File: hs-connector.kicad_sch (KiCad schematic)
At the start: 48 parts, among them J2001 Socket_Samtec_ERF8_2x25_ERF8-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, T2001 Choke_DLW21SN900HQ2L, T2002 Choke_DLW21SN900HQ2L, T2003 Choke_DLW21SN900HQ2L, U2001 SN65MLVD200A, U2002 74AVC4T245_UQFN

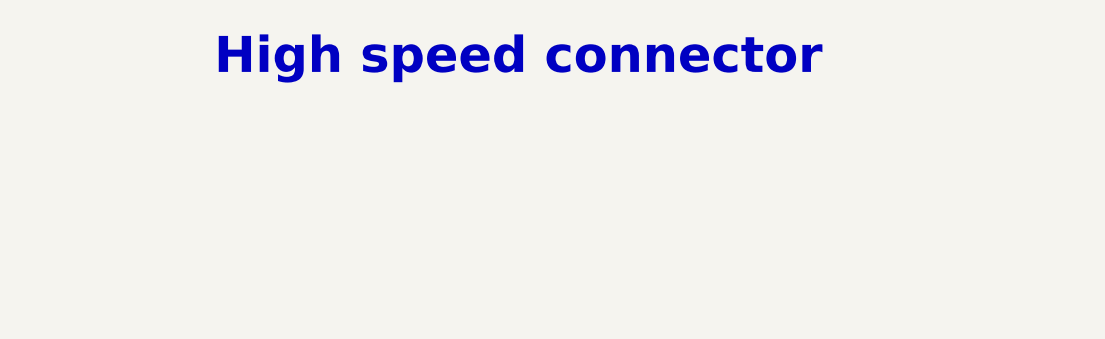
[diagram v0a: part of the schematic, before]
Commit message: [#100282] Add missing schematic sheet names and align them all
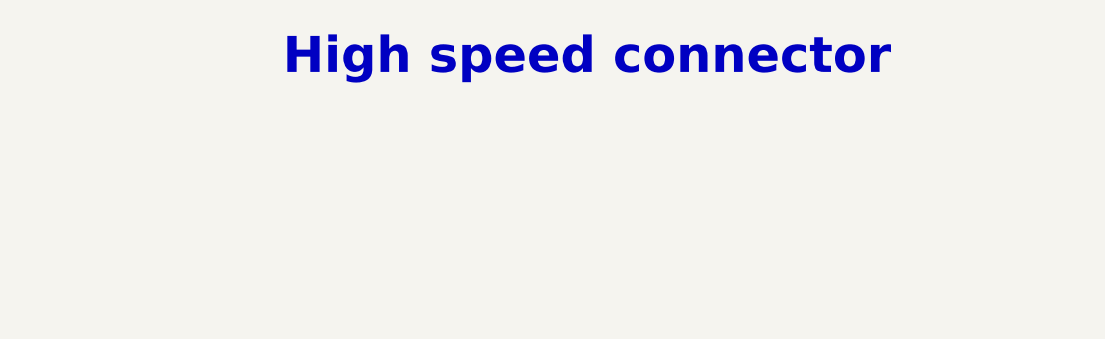
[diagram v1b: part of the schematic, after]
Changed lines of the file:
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@@
 	(text "High speed connector"
 		(exclude_from_sim no)
-		(at 203.2 38.1 0)
+		(at 210.82 38.1 0)
 		(effects
 			(font

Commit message: [#100501] Reannotate schematic
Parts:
- renumbered C2019 to C181, C2020 to C182, C2005 to C183, C2006 to C184, C2007 to C185, C2008 to C186, C2009 to C187, C2001 to C188, C2003 to C189, C2002 to C190, C2004 to C191, C2010 to C192, C2011 to C193, C2012 to C194, C2013 to C195, C2014 to C196, C2015 to C197, C2016 to C198, C2017 to C199, C2018 to C200, D2001 to D1, F2001 to F1, J2001 to J6, R2019 to R219, R2001 to R220, R2002 to R221, R2003 to R222, R2004 to R223, R2005 to R224, R2006 to R225, R2007 to R226, R2008 to R227, R2009 to R228, R2010 to R229, R2011 to R230, R2012 to R231, R2013 to R232, R2014 to R233, R2015 to R234, R2016 to R235, R2017 to R236, R2018 to R237, R2020 to R238, T2001 to T1, T2002 to T2, T2003 to T3, U2002 to U27, U2001 to U28

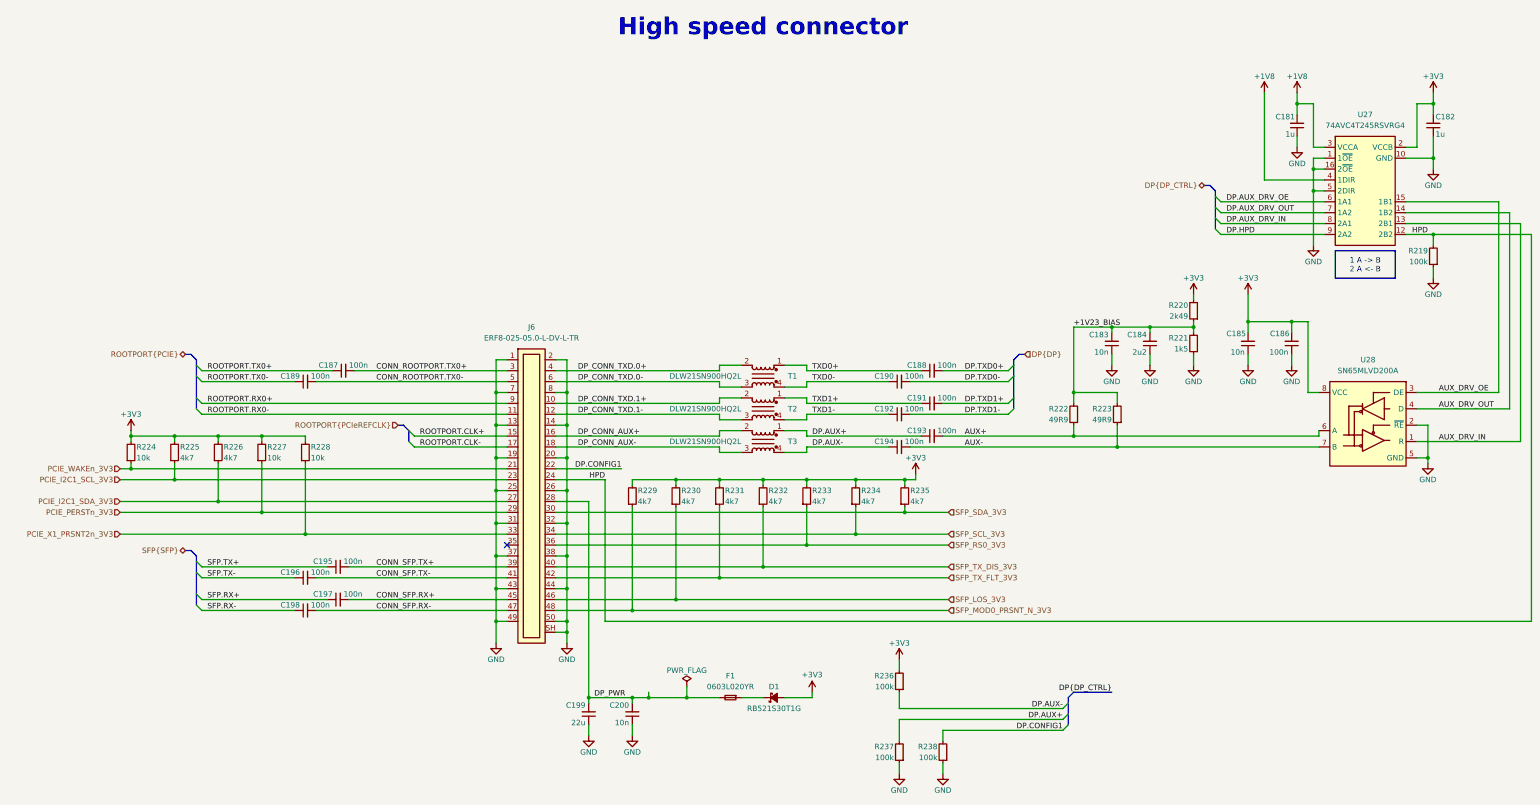
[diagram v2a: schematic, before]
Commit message: [#100595] Update connections according to client request
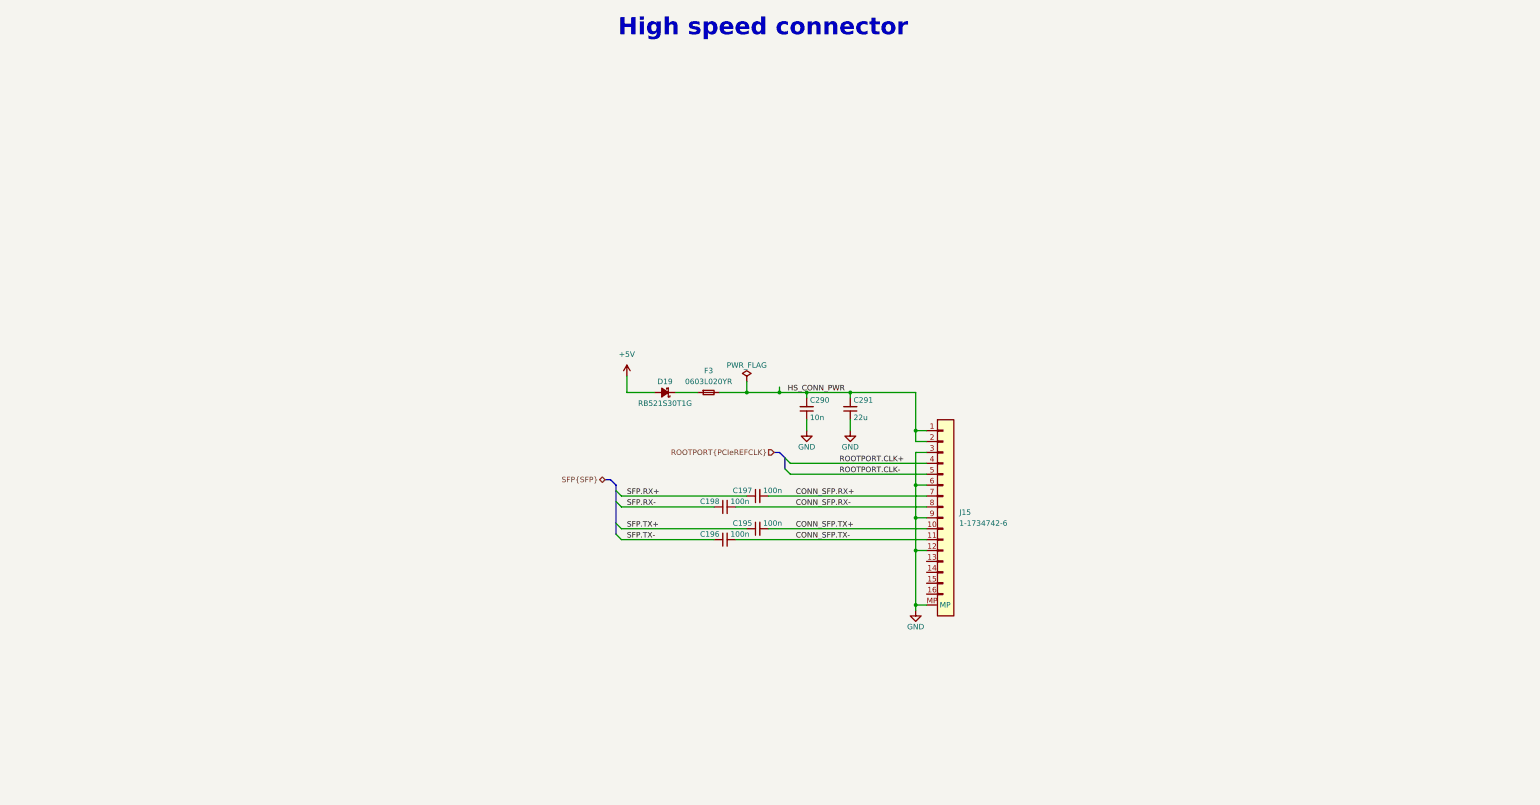
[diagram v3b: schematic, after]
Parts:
- removed C181, C182: C_1u_0402, antmicro-footprints:C_0402_1005Metric, symbol antmicroCapacitors0402:C_1u_0402
- removed C183, C185, C200: C_10n_0402, antmicro-footprints:C_0402_1005Metric, symbol antmicroCapacitors0402:C_10n_0402
- removed C184: C_2u2_0402, antmicro-footprints:C_0402_1005Metric, symbol antmicroCapacitors0402:C_2u2_0402
- removed C186, C187, C188, C189, C190, C191, C192, C193, C194: C_100n_0402, antmicro-footprints:C_0402_1005Metric, symbol antmicroCapacitors0402:C_100n_0402
- removed C199: C_22u_16V_0603, antmicro-footprints:C_0603_1608Metric_EIA, symbol antmicroCapacitors0603:C_22u_16V_0603
- removed D1: RB521S30T1G, antmicro-footprints:SOD-523, symbol antmicroDiodesRectifiersSingle:RB521S30T1G
- removed F1: PTC_500mA_0603, antmicro-footprints:F_0603_1608Metric, symbol antmicroFuses:PTC_500mA_0603
- removed J6: Socket_Samtec_ERF8_2x25_ERF8-025-05.0-L-DV-L-TR, antmicro-footprints:Conn_Socket_Samtec_ERF8_2x25_ERF8-025-05.0-L-DV-L-TR, symbol antmicroB2BConnectors:Socket_Samtec_ERF8_2x25_ERF8-025-05.0-L-DV-L-TR
- removed R219, R236, R237, R238: R_100k_0402, antmicro-footprints:R_0402_1005Metric, symbol antmicroResistors0402:R_100k_0402
- removed R220: R_2k49_0402, antmicro-footprints:R_0402_1005Metric, symbol antmicroResistors0402:R_2k49_0402
- removed R221: R_1k5_0402, antmicro-footprints:R_0402_1005Metric, symbol antmicroResistors0402:R_1k5_0402
- removed R222, R223: R_49R9_0402, antmicro-footprints:R_0402_1005Metric, symbol antmicroResistors0402:R_49R9_0402
- removed R224, R227, R228: R_10k_0402, antmicro-footprints:R_0402_1005Metric, symbol antmicroResistors0402:R_10k_0402
- removed R225, R226, R229, R230, R231, R232, R233, R234, R235: R_4k7_0402, antmicro-footprints:R_0402_1005Metric, symbol antmicroResistors0402:R_4k7_0402
- removed T1, T2, T3: Choke_DLW21SN900HQ2L, antmicro-footprints:Choke_Murata-DLW21, symbol antmicroCommonModeChokes:Choke_DLW21SN900HQ2L
- removed U27: 74AVC4T245_UQFN, antmicro-footprints:UQFN-16-1.8x2.6mm_P0.4mm_Texas_RSV0016A, symbol antmicroLogicTranslatorsLevelShifters:74AVC4T245_UQFN
- removed U28: SN65MLVD200A, antmicro-footprints:SOIC-8_3.9x4.9x1.75mm_P1.27mm, symbol antmicroInterfaceDriversReceiversTransceivers:SN65MLVD200A
- added C290: C_10n_0402, antmicro-footprints:C_0402_1005Metric, symbol antmicroCapacitors0402:C_10n_0402
- added C291: C_22u_16V_0603, antmicro-footprints:C_0603_1608Metric_EIA, symbol antmicroCapacitors0603:C_22u_16V_0603
- added D19: RB521S30T1G, antmicro-footprints:SOD-523, symbol antmicroDiodesRectifiersSingle:RB521S30T1G
- added F3: PTC_500mA_0603, antmicro-footprints:F_0603_1608Metric, symbol antmicroFuses:PTC_500mA_0603
- added J15: FFC_TE_1-1734742-6, antmicro-footprints:Conn_FFC_TE_1-1734742-6, symbol antmicroFCCConnectors:FFC_TE_1-1734742-6
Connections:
- net CONN_SFP.RX+: now also J15.7
- net CONN_SFP.RX-: now also J15.8
- net CONN_SFP.TX+: now also J15.10
- net CONN_SFP.TX-: now also J15.11
- net GND: now also C290.1, C291.1, J15.12, J15.3, J15.6, J15.9, J15.MP
- net ROOTPORT.CLK+: now also J15.4
- net ROOTPORT.CLK-: now also J15.5
- new net: D19.1 (C), F3.1
- new net +5V: D19.2 (A)
- new net HS_CONN_PWR: C290.2, C291.2, F3.2, J15.1, J15.2
- no-connect marks 1 -> 0

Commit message: [#100595] Update HS connections
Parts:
- removed D19: RB521S30T1G, antmicro-footprints:SOD-523, symbol antmicroDiodesRectifiersSingle:RB521S30T1G
- added D23: RB521S30T1G, antmicro-footprints:SOD-523, symbol antmicroDiodesRectifiersSingle:RB521S30T1G
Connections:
- net +5V: now also D23.2 (A)
- net at F3.1: now also D23.1 (C)
- net PCIE_PWR_EN: now reaches J15.13
- net PCIE_DET_WAKE: now reaches J15.14
- net PCIE_CLKREQ_N: now reaches J15.15
- net PCIE_RST_B: now reaches J15.16
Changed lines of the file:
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@@
+	(wire
+		(pts
+			(xy 242.57 165.1) (xy 248.92 165.1)
+		)
+		(stroke
+			(width 0)
+			(type default)
+		)
+	)
 	(wire
 		(pts
@@
 	(wire
 		(pts
+			(xy 242.57 162.56) (xy 248.92 162.56)
+		)
+		(stroke
+			(width 0)
+			(type default)
+		)
+	)
+	(wire
+		(pts
 			(xy 212.09 147.32) (xy 248.92 147.32)
 		)
@@
 	(wire
 		(pts
+			(xy 242.57 167.64) (xy 248.92 167.64)
+		)
+		(stroke
+			(width 0)
+			(type default)
+		)
+	)
+	(wire
+		(pts
 			(xy 248.92 137.16) (xy 246.38 137.16)
 		)
@@
 		(pts
 			(xy 246.38 172.72) (xy 248.92 172.72)
+		)
+		(stroke
+			(width 0)
+			(type default)
+		)
+	)
+	(wire
+		(pts
+			(xy 242.57 170.18) (xy 248.92 170.18)
 		)
 		(stroke
@@
 		(shape bidirectional)
 		(at 173.99 143.51 180)
+		(effects
+			(font
+				(size 1.27 1.27)
+			)
+			(justify right)
+		)
+	)
+	(hierarchical_label "PCIE_PWR_EN"
+		(shape input)
+		(at 242.57 162.56 180)
+		(effects
+			(font
+				(size 1.27 1.27)
+			)
+			(justify right)
+		)
+	)
+	(hierarchical_label "PCIE_CLKREQ_N"
+		(shape input)
+		(at 242.57 167.64 180)
+		(effects
+			(font
+				(size 1.27 1.27)
+			)
+			(justify right)
+		)
+	)
+	(hierarchical_label "PCIE_DET_WAKE"
+		(shape input)
+		(at 242.57 165.1 180)
+		(effects
+			(font
+				(size 1.27 1.27)
+			)
+			(justify right)
+		)
+	)
+	(hierarchical_label "PCIE_RST_B"
+		(shape input)
+		(at 242.57 170.18 180)
 		(effects
 			(font
@@
 	)
 	(symbol
+		(lib_id "antmicroDiodesRectifiersSingle:RB521S30T1G")
+		(at 190.5 123.19 180)
+		(unit 1)
+		(body_style 1)
+		(exclude_from_sim no)
+		(in_bom yes)
+		(on_board yes)
+		(in_pos_files yes)
+		(dnp no)
+		(property "Reference" "D23"
+			(at 187.96 120.65 0)
+			(show_name no)
+			(do_not_autoplace no)
+			(effects
+				(font
+					(size 1.27 1.27)
+					(thickness 0.15)
+				)
+			)
+		)
+		(property "Value" "RB521S30T1G"
+			(at 167.64 107.95 0)
+			(hide yes)
+			(show_name no)
+			(do_not_autoplace no)
+			(effects
+				(font
+					(size 1.27 1.27)
+					(thickness 0.15)
+				)
+				(justify left bottom)
+			)
+		)
+		(property "Footprint" "antmicro-footprints:SOD-523"
+			(at 167.64 113.03 0)
+			(hide yes)
+			(show_name no)
+			(do_not_autoplace no)
+			(effects
+				(font
+					(size 1.27 1.27)
+					(thickness 0.15)
+				)
+				(justify left bottom)
+			)
+		)
+		(property "Datasheet" "https://www.onsemi.com/pdf/datasheet/rb521s30t1-d.pdf"
+			(at 167.64 110.49 0)
+			(hide yes)
+			(show_name no)
+			(do_not_autoplace no)
+			(effects
+				(font
+					(size 1.27 1.27)
+					(thickness 0.15)
+				)
+				(justify left bottom)
+			)
+		)
+		(property "Description" "Small Signal Schottky Diode, Single, 30 V, 200 mA, 500 mV, 1 A, 125 °C"
+			(at 190.5 123.19 0)
+			(hide yes)
+			(show_name no)
+			(do_not_autoplace no)
+			(effects
+				(font
+					(size 1.27 1.27)
+				)
+			)
+		)
+		(property "MPN" "RB521S30T1G"
+			(at 187.96 125.73 0)
+			(show_name no)
+			(do_not_autoplace no)
+			(effects
+				(font
+					(size 1.27 1.27)
+					(thickness 0.15)
+				)
+			)
+		)
+		(property "Manufacturer" "ON Semiconductor"
+			(at 167.64 105.41 0)
+			(hide yes)
+			(show_name no)
+			(do_not_autoplace no)
+			(effects
+				(font
+					(size 1.27 1.27)
+					(thickness 0.15)
+				)
+				(justify left bottom)
+			)
+		)
+		(property "Author" "Antmicro"
+			(at 167.64 102.87 0)
+			(hide yes)
+			(show_name no)
+			(do_not_autoplace no)
+			(effects
+				(font
+					(size 1.27 1.27)
+					(thickness 0.15)
+				)
+				(justify left bottom)
+			)
+		)
+		(property "License" "Apache-2.0"
+			(at 167.64 100.33 0)
+			(hide yes)
+			(show_name no)
+			(do_not_autoplace no)
+			(effects
+				(font
+					(size 1.27 1.27)
+					(thickness 0.15)
+				)
+				(justify left bottom)
+			)
+		)
+		(pin "1"
+		)
+		(pin "2"
+		)
+		(instances
+			(project "altera-modular-agilex-5-dc-scm"
+				(path "/6bb9d978-a328-4b30-874b-55170a976185/24358ccd-38f4-4473-b406-ebc28282868f"
+					(reference "D23")
+					(unit 1)
+				)
+			)
+		)
+	)
+	(symbol
 		(lib_id "antmicropower:GND")
 		(at 220.98 132.08 0)
@@
 					(unit 1)
 				)
-			)
-		)
-	)
-	(symbol
-		(lib_id "antmicroDiodesRectifiersSingle:RB521S30T1G")
-		(at 190.5 123.19 180)
-		(unit 1)
-		(body_style 1)
-		(exclude_from_sim no)
-		(in_bom yes)
-		(on_board yes)
-		(in_pos_files yes)
-		(dnp no)
-		(property "Reference" "D19"
-			(at 187.96 120.65 0)
-			(show_name no)
-			(do_not_autoplace no)
-			(effects
-				(font
-					(size 1.27 1.27)
-					(thickness 0.15)
-				)
-			)
-		)
-		(property "Value" "RB521S30T1G"
-			(at 167.64 107.95 0)
-			(hide yes)
-			(show_name no)
-			(do_not_autoplace no)
-			(effects
-				(font
-					(size 1.27 1.27)
-					(thickness 0.15)
-				)
-				(justify left bottom)
-			)
-		)
-		(property "Footprint" "antmicro-footprints:SOD-523"
-			(at 167.64 113.03 0)
-			(hide yes)
-			(show_name no)
-			(do_not_autoplace no)
-			(effects
-				(font
-					(size 1.27 1.27)
-					(thickness 0.15)
-				)
-				(justify left bottom)
-			)
-		)
-		(property "Datasheet" "https://www.onsemi.com/pdf/datasheet/rb521s30t1-d.pdf"
-			(at 167.64 110.49 0)
-			(hide yes)
-			(show_name no)
-			(do_not_autoplace no)
-			(effects
-				(font
-					(size 1.27 1.27)
-					(thickness 0.15)
-				)
-				(justify left bottom)
-			)
-		)
-		(property "Description" "Small Signal Schottky Diode, Single, 30 V, 200 mA, 500 mV, 1 A, 125 °C"
-			(at 190.5 123.19 0)
-			(hide yes)
-			(show_name no)
-			(do_not_autoplace no)
-			(effects
-				(font
-					(size 1.27 1.27)
-				)
-			)
-		)
-		(property "MPN" "RB521S30T1G"
-			(at 187.96 125.73 0)
-			(show_name no)
-			(do_not_autoplace no)
-			(effects
-				(font
-					(size 1.27 1.27)
-					(thickness 0.15)
-				)
-			)
-		)
-		(property "Manufacturer" "ON Semiconductor"
-			(at 167.64 105.41 0)
-			(hide yes)
-			(show_name no)
-			(do_not_autoplace no)
-			(effects
-				(font
-					(size 1.27 1.27)
-					(thickness 0.15)
-				)
-				(justify left bottom)
-			)
-		)
-		(property "Author" "Antmicro"
-			(at 167.64 102.87 0)
-			(hide yes)
-			(show_name no)
-			(do_not_autoplace no)
-			(effects
-				(font
-					(size 1.27 1.27)
-					(thickness 0.15)
-				)
-				(justify left bottom)
-			)
-		)
-		(property "License" "Apache-2.0"
-			(at 167.64 100.33 0)
-			(hide yes)
-			(show_name no)
-			(do_not_autoplace no)
-			(effects
-				(font
-					(size 1.27 1.27)
-					(thickness 0.15)
-				)
-				(justify left bottom)
-			)
-		)
-		(pin "1"
-		)
-		(pin "2"
-		)
-		(instances
-			(project "altera-modular-agilex-5-dc-scm"
-				(path "/6bb9d978-a328-4b30-874b-55170a976185/24358ccd-38f4-4473-b406-ebc28282868f"
-					(reference "D19")
-					(unit 1)
-				)

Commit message: [#100501] Reannotate schematic
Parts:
- renumbered C290 to C186, C291 to C187, C197 to C188, C198 to C189, C195 to C190, C196 to C191, D23 to D6, F3 to F1, J15 to J7
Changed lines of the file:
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@@
 		(in_pos_files yes)
 		(dnp no)
-		(property "Reference" "C196"
+		(property "Reference" "C191"
 			(at 200.66 156.21 0)
 			(show_name no)
@@
 			(project "altera-modular-agilex-5-dc-scm"
 				(path "/6bb9d978-a328-4b30-874b-55170a976185/24358ccd-38f4-4473-b406-ebc28282868f"
-					(reference "C196")
+					(reference "C191")
 					(unit 1)
 				)
@@
 		(in_pos_files yes)
 		(dnp no)
-		(property "Reference" "C290"
+		(property "Reference" "C186"
 			(at 221.742 124.968 90)
 			(show_name no)
@@
 			(project "altera-modular-agilex-5-dc-scm"
 				(path "/6bb9d978-a328-4b30-874b-55170a976185/24358ccd-38f4-4473-b406-ebc28282868f"
-					(reference "C290")
+					(reference "C186")
 					(unit 1)
 				)
@@
 		(in_pos_files yes)
 		(dnp no)
-		(property "Reference" "C195"
+		(property "Reference" "C190"
 			(at 208.28 153.67 0)
 			(show_name no)
@@
 			(project "altera-modular-agilex-5-dc-scm"
 				(path "/6bb9d978-a328-4b30-874b-55170a976185/24358ccd-38f4-4473-b406-ebc28282868f"
-					(reference "C195")
+					(reference "C190")
 					(unit 1)
 				)
@@
 		(dnp no)
 		(fields_autoplaced yes)
-		(property "Reference" "F3"
+		(property "Reference" "F1"
 			(at 198.12 118.11 0)
 			(show_name no)
@@
 			(project "altera-modular-agilex-5-dc-scm"
 				(path "/6bb9d978-a328-4b30-874b-55170a976185/24358ccd-38f4-4473-b406-ebc28282868f"
-					(reference "F3")
+					(reference "F1")
 					(unit 1)
 				)
@@
 		(in_pos_files yes)
 		(dnp no)
-		(property "Reference" "D23"
+		(property "Reference" "D6"
 			(at 187.96 120.65 0)
 			(show_name no)
@@
 			(project "altera-modular-agilex-5-dc-scm"
 				(path "/6bb9d978-a328-4b30-874b-55170a976185/24358ccd-38f4-4473-b406-ebc28282868f"
-					(reference "D23")
+					(reference "D6")
 					(unit 1)
 				)
@@
 		(in_pos_files yes)
 		(dnp no)
-		(property "Reference" "#PWR0309"
+		(property "Reference" "#PWR0293"
 			(at 229.87 134.62 0)
 			(hide yes)
@@
 			(project "altera-modular-agilex-5-dc-scm"
 				(path "/6bb9d978-a328-4b30-874b-55170a976185/24358ccd-38f4-4473-b406-ebc28282868f"
-					(reference "#PWR0309")
+					(reference "#PWR0293")
 					(unit 1)
 				)
@@
 		(dnp no)
 		(fields_autoplaced yes)
-		(property "Reference" "J15"
+		(property "Reference" "J7"
 			(at 256.54 151.13 0)
 			(show_name no)
@@
 			(project "altera-modular-agilex-5-dc-scm"
 				(path "/6bb9d978-a328-4b30-874b-55170a976185/24358ccd-38f4-4473-b406-ebc28282868f"
-					(reference "J15")
+					(reference "J7")
 					(unit 1)
 				)
@@
 		(in_pos_files yes)
 		(dnp no)
-		(property "Reference" "#PWR0308"
+		(property "Reference" "#PWR0294"
 			(at 240.03 134.62 0)
 			(hide yes)
@@
 			(project "altera-modular-agilex-5-dc-scm"
 				(path "/6bb9d978-a328-4b30-874b-55170a976185/24358ccd-38f4-4473-b406-ebc28282868f"
-					(reference "#PWR0308")
+					(reference "#PWR0294")
 					(unit 1)
 				)
@@
 		(in_pos_files yes)
 		(dnp no)
-		(property "Reference" "C291"
+		(property "Reference" "C187"
 			(at 231.902 124.968 90)
 			(show_name no)
@@
 			(project "altera-modular-agilex-5-dc-scm"
 				(path "/6bb9d978-a328-4b30-874b-55170a976185/24358ccd-38f4-4473-b406-ebc28282868f"
-					(reference "C291")
+					(reference "C187")
 					(unit 1)
 				)
@@
 		(in_pos_files yes)
 		(dnp no)
-		(property "Reference" "C198"
+		(property "Reference" "C189"
 			(at 200.66 148.59 0)
 			(show_name no)
@@
 			(project "altera-modular-agilex-5-dc-scm"
 				(path "/6bb9d978-a328-4b30-874b-55170a976185/24358ccd-38f4-4473-b406-ebc28282868f"
-					(reference "C198")
+					(reference "C189")
 					(unit 1)
 				)
@@
 		(dnp no)
 		(fields_autoplaced yes)
-		(property "Reference" "#PWR0285"
+		(property "Reference" "#PWR0292"
 			(at 194.31 121.92 0)
 			(hide yes)
@@
 			(project "altera-modular-agilex-5-dc-scm"
 				(path "/6bb9d978-a328-4b30-874b-55170a976185/24358ccd-38f4-4473-b406-ebc28282868f"
-					(reference "#PWR0285")
+					(reference "#PWR0292")
 					(unit 1)
 				)
@@
 		(in_pos_files yes)
 		(dnp no)
-		(property "Reference" "#FLG025"
+		(property "Reference" "#FLG018"
 			(at 207.01 118.745 0)
 			(hide yes)
@@
 			(project "altera-modular-agilex-5-dc-scm"
 				(path "/6bb9d978-a328-4b30-874b-55170a976185/24358ccd-38f4-4473-b406-ebc28282868f"
-					(reference "#FLG025")
+					(reference "#FLG018")
 					(unit 1)
 				)
@@
 		(in_pos_files yes)
 		(dnp no)
-		(property "Reference" "#PWR0465"
+		(property "Reference" "#PWR0295"
 			(at 237.49 176.53 0)
 			(hide yes)
@@
 			(project "altera-modular-agilex-5-dc-scm"
 				(path "/6bb9d978-a328-4b30-874b-55170a976185/24358ccd-38f4-4473-b406-ebc28282868f"
-					(reference "#PWR0465")
+					(reference "#PWR0295")
 					(unit 1)
 				)
@@
 		(in_pos_files yes)
 		(dnp no)
-		(property "Reference" "C197"
+		(property "Reference" "C188"
 			(at 208.28 146.05 0)
 			(show_name no)
@@
 			(project "altera-modular-agilex-5-dc-scm"
 				(path "/6bb9d978-a328-4b30-874b-55170a976185/24358ccd-38f4-4473-b406-ebc28282868f"
-					(reference "C197")
+					(reference "C188")
 					(unit 1)
 				)
